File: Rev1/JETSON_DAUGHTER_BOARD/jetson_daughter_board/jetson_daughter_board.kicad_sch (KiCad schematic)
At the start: 2 parts, among them J1 F3311A7H121014E200, J2 TFML-105-01-L-D-RA

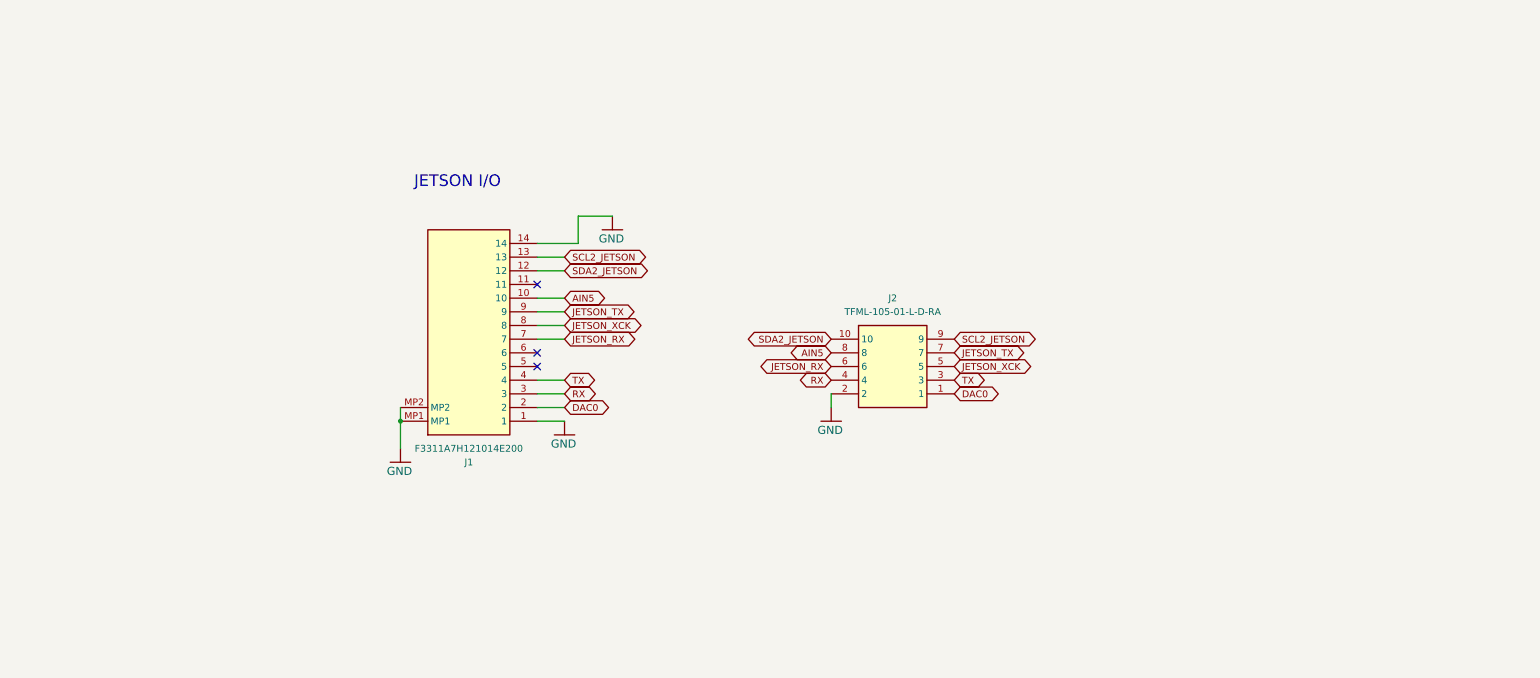
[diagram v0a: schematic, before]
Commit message: Updated USB HUB
Based on Mechanical Feedback
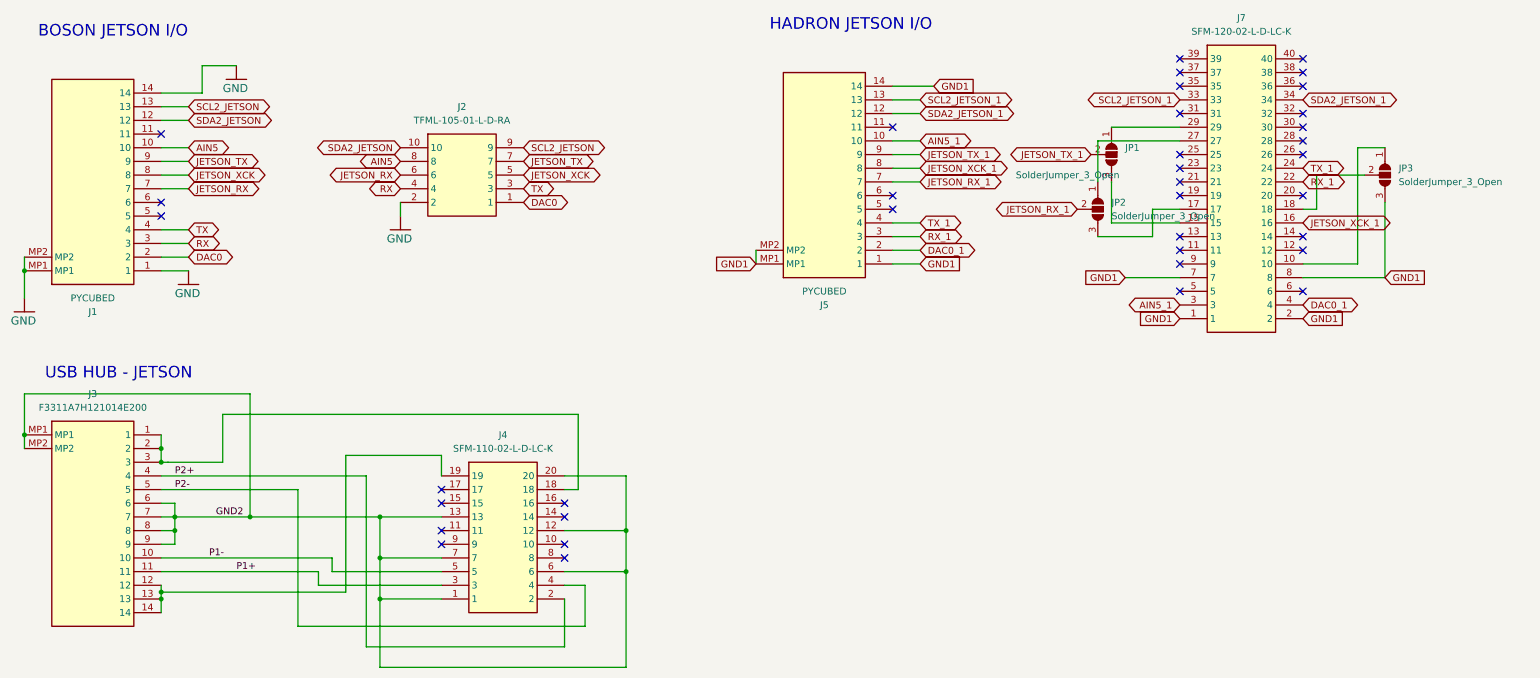
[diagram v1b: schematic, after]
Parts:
- added J3: F3311A7H121014E200, F3311A7H121014E200, symbol SamacSys_Parts:F3311A7H121014E200
- added J4: SFM-110-02-L-D-LC-K, SFM11002LDLCK, symbol SamacSys_Parts:SFM-110-02-L-D-LC-K
- added J5: PYCUBED, F3311A7H121014E200, symbol SamacSys_Parts:F3311A7H121014E200
- added J7: SFM-120-02-L-D-LC-K, SFM12002LDLCK, symbol SamacSys_Parts:SFM-120-02-L-D-LC-K
- added JP1, JP2, JP3: SolderJumper_3_Open, Jumper:SolderJumper-3_P1.3mm_Open_Pad1.0x1.5mm, symbol Jumper:SolderJumper_3_Open
- J1: value F3311A7H121014E200 -> PYCUBED
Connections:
- new net: J7.27, JP2.1 (A)
- new net: J7.17, JP2.3 (B)
- new net: J3.1, J3.2, J3.3, J4.18
- new net: J3.12, J3.13, J3.14, J4.19
- new net: J7.29, JP1.1 (A)
- new net: J7.15, JP1.3 (B)
- new net: J7.10, JP3.1 (A)
- new net: J7.18, JP3.2 (C)
- new net AIN5_1: J5.10, J7.3
- new net DAC0_1: J5.2, J7.4
- new net GND1: J5.1, J5.14, J5.MP1, J5.MP2, J7.1, J7.2, J7.7, J7.8, JP3.3 (B)
- new net GND2: J3.6, J3.7, J3.8, J3.9, J3.MP1, J3.MP2, J4.1, J4.12, J4.13, J4.20, J4.6, J4.7
- new net JETSON_RX_1: J5.7, JP2.2 (C)
- new net JETSON_TX_1: J5.9, JP1.2 (C)
- new net JETSON_XCK_1: J5.8, J7.16
- new net P1+: J3.11, J4.3
- new net P1-: J3.10, J4.5
- new net P2+: J3.4, J4.2
- new net P2-: J3.5, J4.4
- new net RX_1: J5.3, J7.22
- new net SCL2_JETSON_1: J5.13, J7.33
- new net SDA2_JETSON_1: J5.12, J7.34
- new net TX_1: J5.4, J7.24
- no-connect marks 3 -> 37
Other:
- note added: "BOSON JETSON I/O"
- note added: "HADRON JETSON I/O"
- note added: "USB HUB - JETSON"
- note removed: "JETSON I/O"
- moved on the sheet: J1, J2

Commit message: Jetson Daughter Board Updated
Added solder jumpers for i2c lines
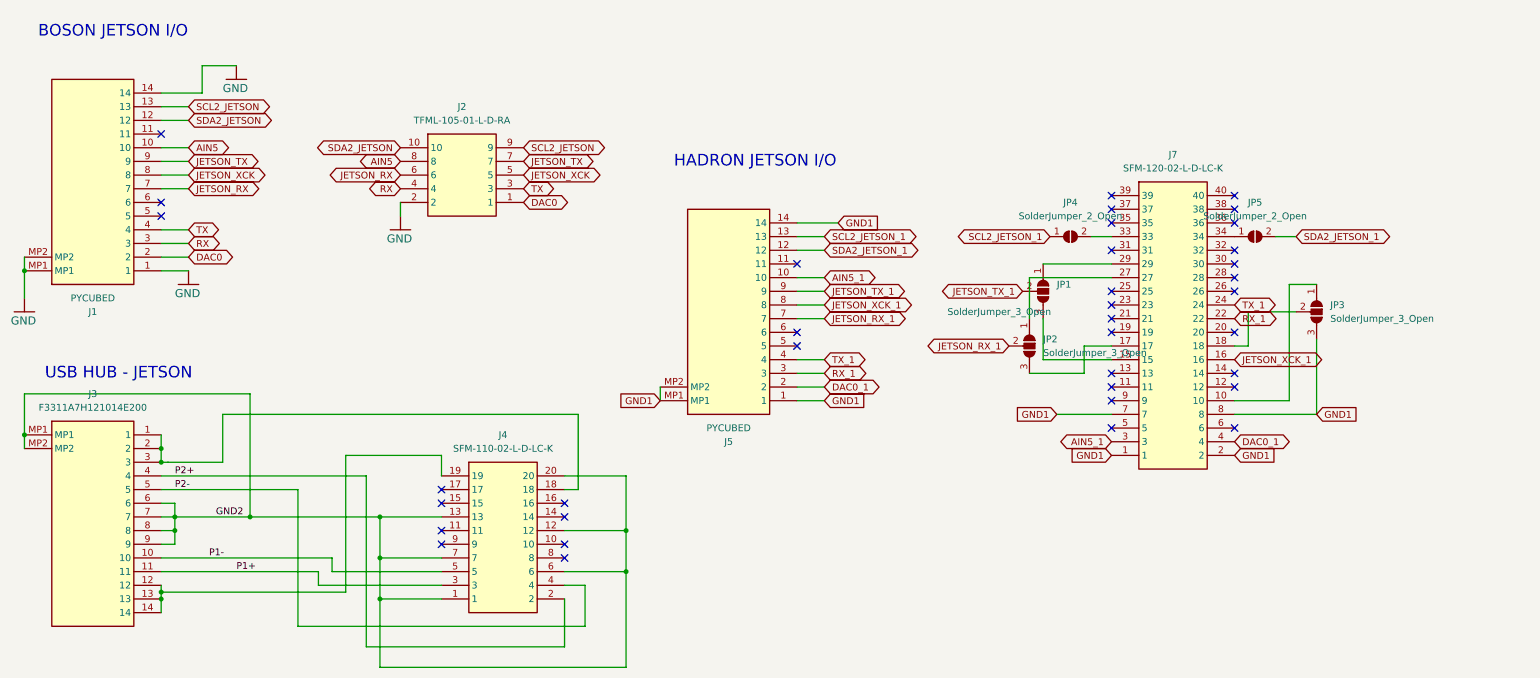
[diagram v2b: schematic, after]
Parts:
- added JP4, JP5: SolderJumper_2_Open, Jumper:SolderJumper-2_P1.3mm_Open_Pad1.0x1.5mm, symbol Jumper:SolderJumper_2_Open
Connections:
- net SCL2_JETSON_1: now also JP4.1 (A); no longer J7.33
- net SDA2_JETSON_1: now also JP5.2 (B); no longer J7.34
- new net: J7.33, JP4.2 (B)
- new net: J7.34, JP5.1 (A)
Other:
- moved on the sheet: J5, J7, JP1, JP2, JP3
